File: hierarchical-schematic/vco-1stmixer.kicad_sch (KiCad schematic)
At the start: 44 parts, among them J101 VCO Control In, J102 1st IF Out, J103 VCO Sample, J104 RF In, J105 Conn_01x02, U101 POS-200, U102 MAV-11, U103 MAV-11, U104 TUF-1H+

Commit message: hierarchical schematic updated to pass erc
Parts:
- JP101: symbol vco-1stmixer:22284028 -> spectrum analyzer:22284028
- U101: symbol vco-1stmixer:POS-200 -> spectrum analyzer:POS-200
- U102, U103: symbol vco-1stmixer:MAV-11 -> spectrum analyzer:MAV-11
- U104: symbol vco-1stmixer:TUF-1H+ -> spectrum analyzer:TUF-1H+
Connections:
- net GND: now also JP101.2 (J2), U104.4 (LO)
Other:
- title: (none) -> Spectrum Analyzer: VCO 1st Mixer
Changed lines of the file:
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@@
   (paper "USLegal")
   (title_block
+    (title "Spectrum Analyzer: VCO 1st Mixer")
+    (date "2022-08-24")
+    (rev "0")
     (company "Andy McCann KA3KAF and Doug McCann KA3KAG")
     (comment 2 "Terry White K7TAU")
@@
   (junction (at 205.74 77.47) (diameter 0) (color 0 0 0 0)
   )
+  (junction (at 226.06 92.71) (diameter 0) (color 0 0 0 0)
+  )
   (junction (at 152.4 180.34) (diameter 0) (color 0 0 0 0)
   )
@@
     (stroke (width 0) (type default) (color 0 0 0 0))
   )
-  (wire (pts (xy 224.79 88.9) (xy 222.25 88.9))
-    (stroke (width 0) (type default) (color 0 0 0 0))
-  )
   (wire (pts (xy 85.09 187.96) (xy 85.09 180.34))
     (stroke (width 0) (type default) (color 0 0 0 0))
   )
+  (wire (pts (xy 226.06 92.71) (xy 237.49 92.71))
+    (stroke (width 0) (type default) (color 0 0 0 0))
+  )
   (wire (pts (xy 222.25 83.82) (xy 222.25 68.58))
     (stroke (width 0) (type default) (color 0 0 0 0))
@@
     (stroke (width 0) (type default) (color 0 0 0 0))
   )
-  (wire (pts (xy 224.79 83.82) (xy 222.25 83.82))
-    (stroke (width 0) (type default) (color 0 0 0 0))
-  )
   (wire (pts (xy 85.09 194.31) (xy 85.09 193.04))
     (stroke (width 0) (type default) (color 0 0 0 0))
@@
     (stroke (width 0) (type default) (color 0 0 0 0))
   )
-  (wire (pts (xy 237.49 92.71) (xy 219.71 92.71))
-    (stroke (width 0) (type default) (color 0 0 0 0))
-  )
   (wire (pts (xy 205.74 92.71) (xy 205.74 87.63))
     (stroke (width 0) (type default) (color 0 0 0 0))
@@
     (stroke (width 0) (type default) (color 0 0 0 0))
   )
-  (wire (pts (xy 261.62 83.82) (xy 237.49 83.82))
+  (wire (pts (xy 261.62 83.82) (xy 241.3 83.82))
     (stroke (width 0) (type default) (color 0 0 0 0))
   )
@@
     (stroke (width 0) (type default) (color 0 0 0 0))
   )
+  (wire (pts (xy 226.06 92.71) (xy 226.06 95.25))
+    (stroke (width 0) (type default) (color 0 0 0 0))
+  )
   (wire (pts (xy 142.24 149.86) (xy 142.24 153.67))
     (stroke (width 0) (type default) (color 0 0 0 0))
@@
     (stroke (width 0) (type default) (color 0 0 0 0))
   )
-  (wire (pts (xy 237.49 88.9) (xy 237.49 92.71))
-    (stroke (width 0) (type default) (color 0 0 0 0))
-  )
   (wire (pts (xy 85.09 140.97) (xy 85.09 180.34))
     (stroke (width 0) (type default) (color 0 0 0 0))
@@
     (stroke (width 0) (type default) (color 0 0 0 0))
   )
+  (wire (pts (xy 219.71 92.71) (xy 226.06 92.71))
+    (stroke (width 0) (type default) (color 0 0 0 0))
+  )
   (wire (pts (xy 199.39 86.36) (xy 199.39 77.47))
     (stroke (width 0) (type default) (color 0 0 0 0))
@@
   )
   (wire (pts (xy 160.02 149.86) (xy 152.4 149.86))
-    (stroke (width 0) (type default) (color 0 0 0 0))
-  )
-  (wire (pts (xy 222.25 88.9) (xy 222.25 95.25))
     (stroke (width 0) (type default) (color 0 0 0 0))
   )
@@
     (effects (font (size 1.27 1.27)) (justify right))
   )
-  (symbol (lib_id "vco-1stmixer:TUF-1H+") (at 231.14 86.36 0) (unit 1)
+  (symbol (lib_id "spectrum analyzer:TUF-1H+") (at 231.14 86.36 0) (unit 1)
     (in_bom yes) (on_board yes)
     (property "Reference" "U104" (id 0) (at 231.14 77.47 0))
     (property "Value" "TUF-1H+" (id 1) (at 231.14 80.01 0))
-    (property "Footprint" "vco-1stmixer:TUF-1H" (id 2) (at 218.44 96.52 0)
-      (effects (font (size 1.27 1.27)) hide)
-    )
-    (property "Datasheet" "https://www.minicircuits.com/pdfs/TUF-1H+.pdf" (id 3) (at 231.14 93.98 0)
+    (property "Footprint" "vco-1stmixer:TUF-1H" (id 2) (at 231.14 86.36 0)
+      (effects (font (size 1.27 1.27)) hide)
+    )
+    (property "Datasheet" "https://www.minicircuits.com/pdfs/TUF-1H+.pdf" (id 3) (at 231.14 86.36 0)
       (effects (font (size 1.27 1.27)) hide)
     )
@@
     (pin "2")
   )
-  (symbol (lib_id "vco-1stmixer:22284028") (at 214.63 92.71 0) (unit 1)
+  (symbol (lib_id "spectrum analyzer:22284028") (at 214.63 92.71 0) (unit 1)
     (in_bom yes) (on_board yes)
     (property "Reference" "JP101" (id 0) (at 214.63 88.9 0))
     (property "Value" "Jumper" (id 1) (at 214.63 96.52 0))
-    (property "Footprint" "vco-1stmixer:22284028" (id 2) (at 214.63 86.614 0)
+    (property "Footprint" "vco-1stmixer:22284028" (id 2) (at 215.9 96.52 0)
       (effects (font (size 1.524 1.524)) hide)
     )
@@
     (pin "1")
   )
-  (symbol (lib_id "vco-1stmixer:MAV-11") (at 185.42 77.47 0) (unit 1)
+  (symbol (lib_id "spectrum analyzer:MAV-11") (at 185.42 77.47 0) (unit 1)
     (in_bom yes) (on_board yes) (fields_autoplaced)
     (property "Reference" "U103" (id 0) (at 198.12 72.8533 0))
@@
     (pin "2")
   )
-  (symbol (lib_name "MAV-11_1") (lib_id "vco-1stmixer:MAV-11") (at 130.81 180.34 0) (unit 1)
+  (symbol (lib_id "spectrum analyzer:MAV-11") (at 130.81 180.34 0) (unit 1)
     (in_bom yes) (on_board yes) (fields_autoplaced)
     (property "Reference" "U102" (id 0) (at 143.51 175.7233 0))
@@
     (pin "2")
   )
-  (symbol (lib_id "power:PWR_FLAG") (at 124.46 87.63 270) (unit 1)
-    (in_bom yes) (on_board yes) (fields_autoplaced)
-    (property "Reference" "#FLG0102" (id 0) (at 126.365 87.63 0)
-      (effects (font (size 1.27 1.27)) hide)
-    )
-    (property "Value" "PWR_FLAG" (id 1) (at 128.27 87.6299 90)
-      (effects (font (size 1.27 1.27)) (justify left))
-    )
-    (property "Footprint" "" (id 2) (at 124.46 87.63 0)
-      (effects (font (size 1.27 1.27)) hide)
-    )
-    (property "Datasheet" "~" (id 3) (at 124.46 87.63 0)
-      (effects (font (size 1.27 1.27)) hide)
-    )
-    (pin "1")
-  )
   (symbol (lib_id "Connector:Conn_Coaxial") (at 205.74 115.57 270) (unit 1)
     (in_bom yes) (on_board yes) (fields_autoplaced)
@@
     (pin "2")
   )
-  (symbol (lib_id "vco-1stmixer:POS-200") (at 106.68 85.09 0) (unit 1)
+  (symbol (lib_id "spectrum analyzer:POS-200") (at 106.68 85.09 0) (unit 1)
     (in_bom yes) (on_board yes)
     (property "Reference" "U101" (id 0) (at 99.06 73.66 0))
     (property "Value" "POS-200" (id 1) (at 111.76 73.66 0))
-    (property "Footprint" "vco-1stmixer:POS-200" (id 2) (at 106.68 82.55 0)
-      (effects (font (size 1.27 1.27)) hide)
-    )
-    (property "Datasheet" "" (id 3) (at 106.68 82.55 0)
+    (property "Footprint" "vco-1stmixer:POS-200" (id 2) (at 106.68 97.79 0)
+      (effects (font (size 1.27 1.27)) hide)
+    )
+    (property "Datasheet" "https://www.mini-circuits.com/pdfs/POS-200+.pdf" (id 3) (at 106.68 96.52 0)
       (effects (font (size 1.27 1.27)) hide)
     )
@@
     (pin "1")
   )
-  (symbol (lib_id "power:GND") (at 222.25 95.25 0) (unit 1)
-    (in_bom yes) (on_board yes) (fields_autoplaced)
-    (property "Reference" "#PWR0120" (id 0) (at 222.25 101.6 0)
-      (effects (font (size 1.27 1.27)) hide)
-    )
-    (property "Value" "GND" (id 1) (at 222.25 100.33 0))
-    (property "Footprint" "" (id 2) (at 222.25 95.25 0)
-      (effects (font (size 1.27 1.27)) hide)
-    )
-    (property "Datasheet" "" (id 3) (at 222.25 95.25 0)
-      (effects (font (size 1.27 1.27)) hide)
-    )
+  (symbol (lib_id "power:GND") (at 226.06 95.25 0) (unit 1)
+    (in_bom yes) (on_board yes) (fields_autoplaced)
+    (property "Reference" "#PWR0120" (id 0) (at 226.06 101.6 0)
+      (effects (font (size 1.27 1.27)) hide)
+    )
+    (property "Value" "GND" (id 1) (at 226.06 100.33 0))
+    (property "Footprint" "" (id 2) (at 226.06 95.25 0)
+      (effects (font (size 1.27 1.27)) hide)
+    )
+    (property "Datasheet" "" (id 3) (at 226.06 95.25 0)
+      (effects (font (size 1.27 1.27)) hide)
+    )

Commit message: appearance improvements
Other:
- moved on the sheet: C101, C102, C103, C104, C105, C106, C107, C108, C109, C110, J101, J102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

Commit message: v7 conversion
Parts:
- J105: Spice_Model Conn_01x02 -> (none); Spice_Netlist_Enabled N -> (none); Spice_Primitive J -> (none)
- JP101: Spice_Model 22284028 -> (none); Spice_Netlist_Enabled N -> (none); Spice_Primitive J -> (none)
- TP101, TP102, TP103, TP104, TP105, TP106: value TestPoint -> ${SIM.PARAMS}; Spice_Netlist_Enabled N -> (none)

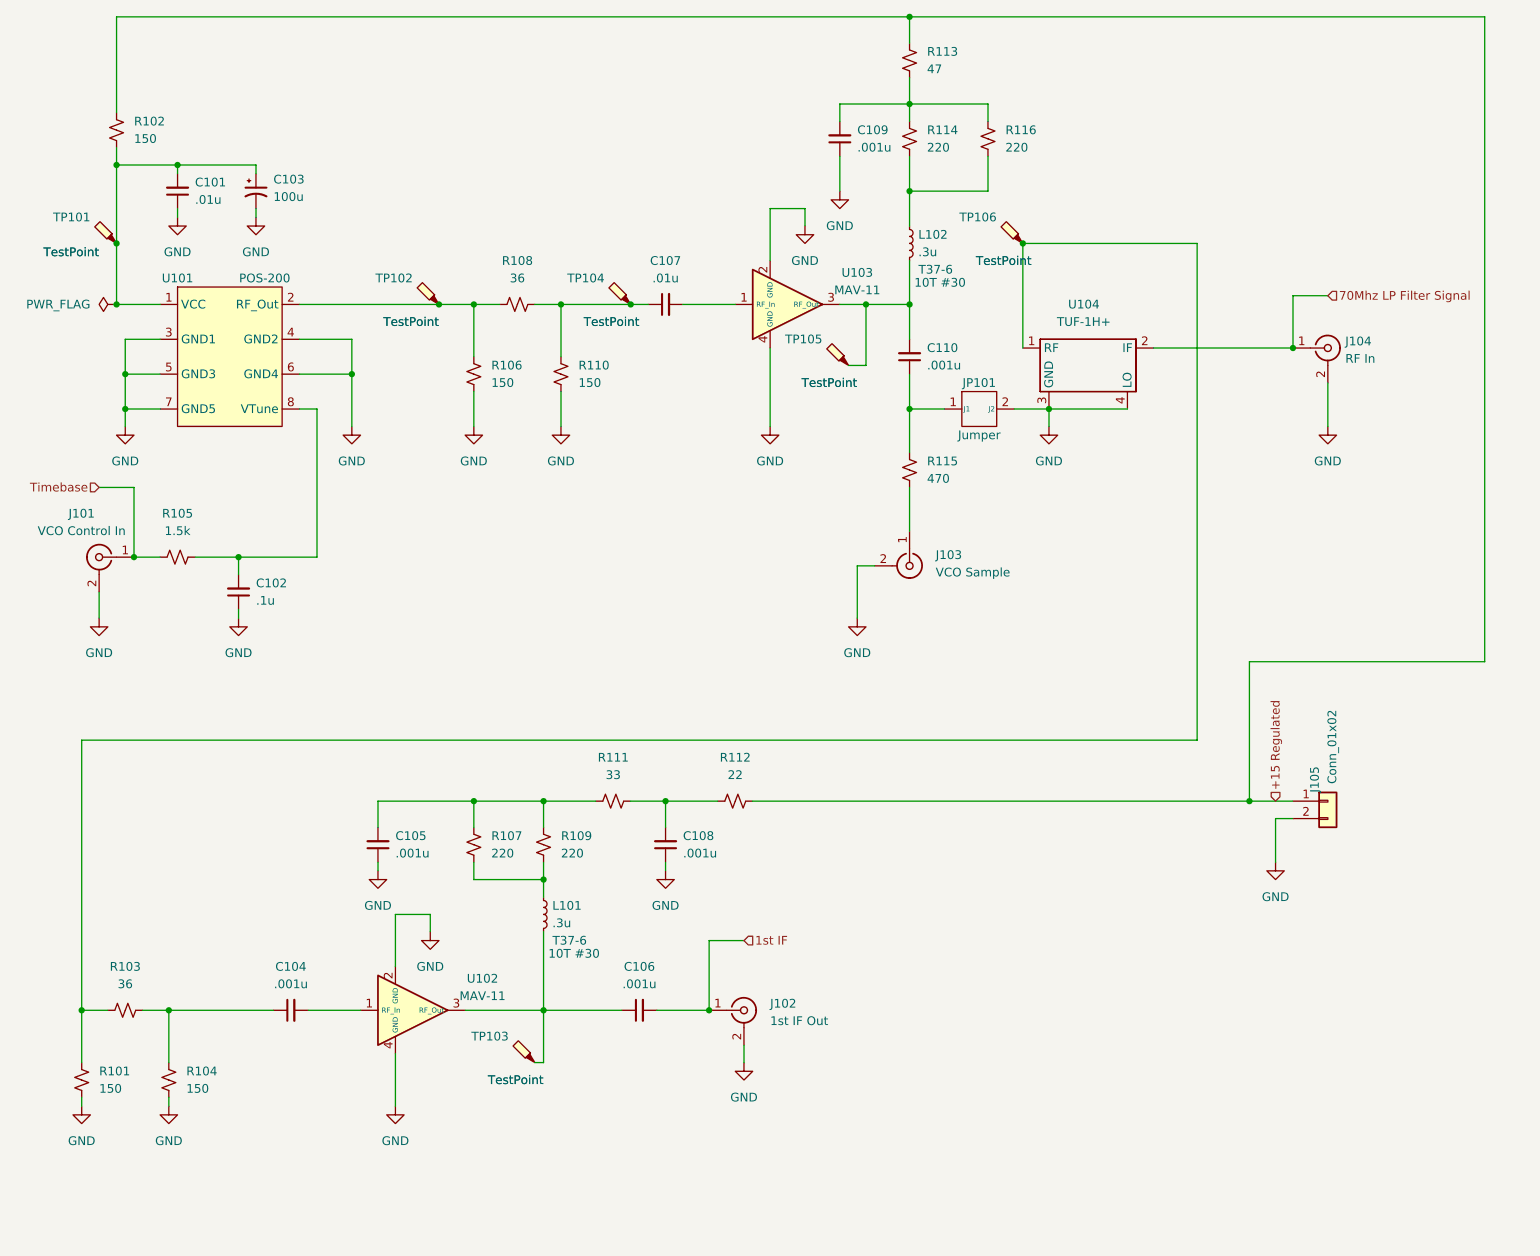
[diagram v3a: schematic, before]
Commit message: Update to timebase and 2lo gerbers
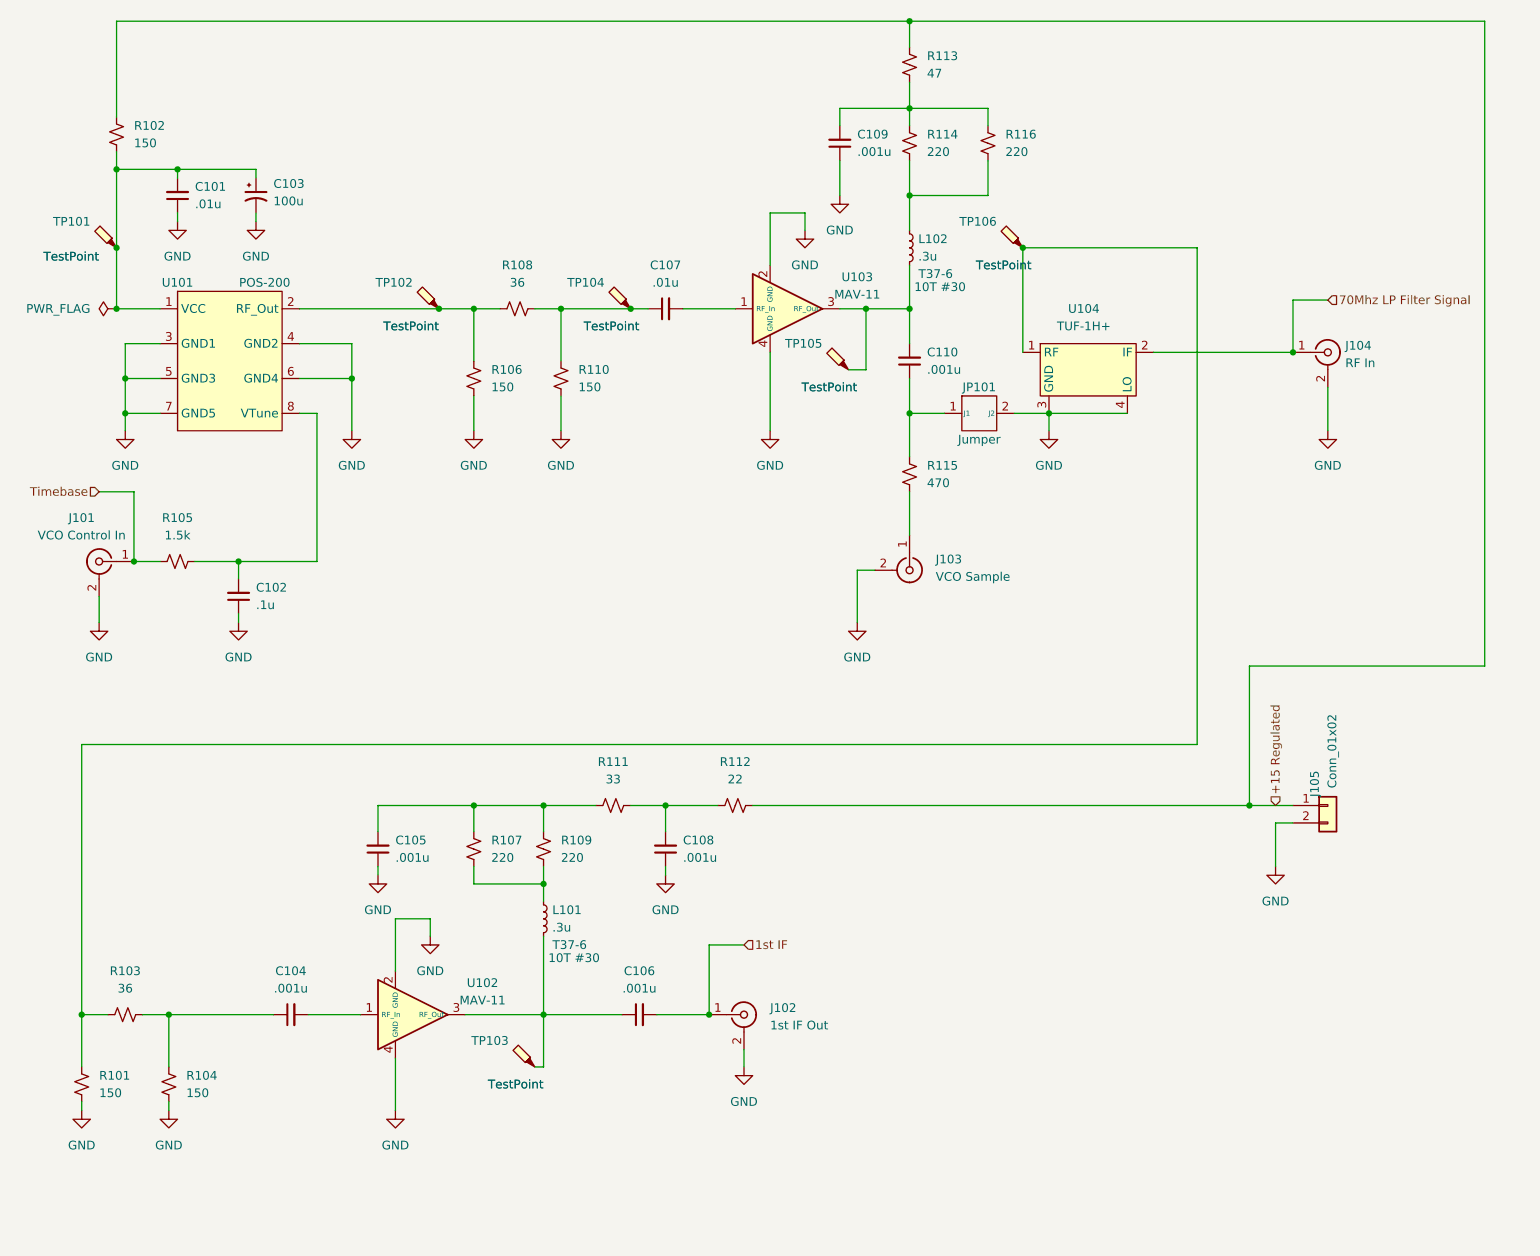
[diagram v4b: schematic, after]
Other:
- moved on the sheet: C101, C102, C103, C104, C105, C106, C107, C108, C109, C110, J101, J102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
